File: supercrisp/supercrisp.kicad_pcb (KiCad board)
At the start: 2 copper layers, 140 x 91 mm, 114 parts, among them P1 USB_C_Plug_USB2.0, P2 USB_C_Plug_USB2.0, SW1 SW_Push, SW10 SW_Push, SW11 SW_Push, SW12 SW_Push, SW13 SW_Push, SW14 SW_Push, SW15 SW_Push, SW16 SW_Push, SW17 SW_Push, SW18 SW_Push, SW19 SW_Push, SW2 SW_Push, SW20 SW_Push, SW21 SW_Push, SW22 SW_Push, SW23 SW_Push, SW24 SW_Push, SW25 SW_Push, SW26 SW_Push, SW3 SW_Push, SW4 SW_Push, SW5 SW_Push, SW6 SW_Push, SW7 SW_Push, SW8 SW_Push, SW9 SW_Push, U1 STM32F072CBTx, U2 USBLC6-2SC6, U3 USBLC6-2SC6, U4 STM32F072CBTx

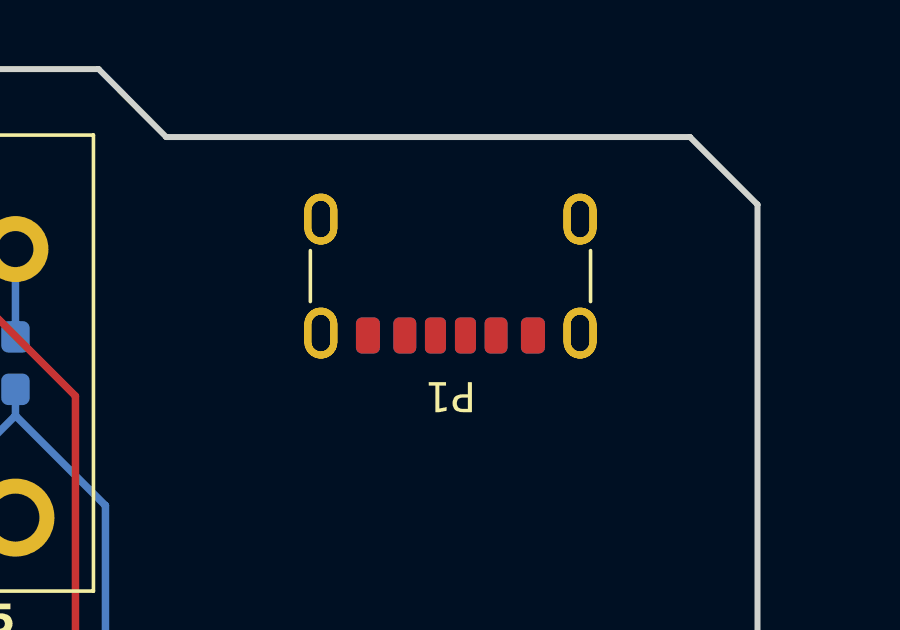
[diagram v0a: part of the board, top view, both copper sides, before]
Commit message: Start adding USB C connector circuit
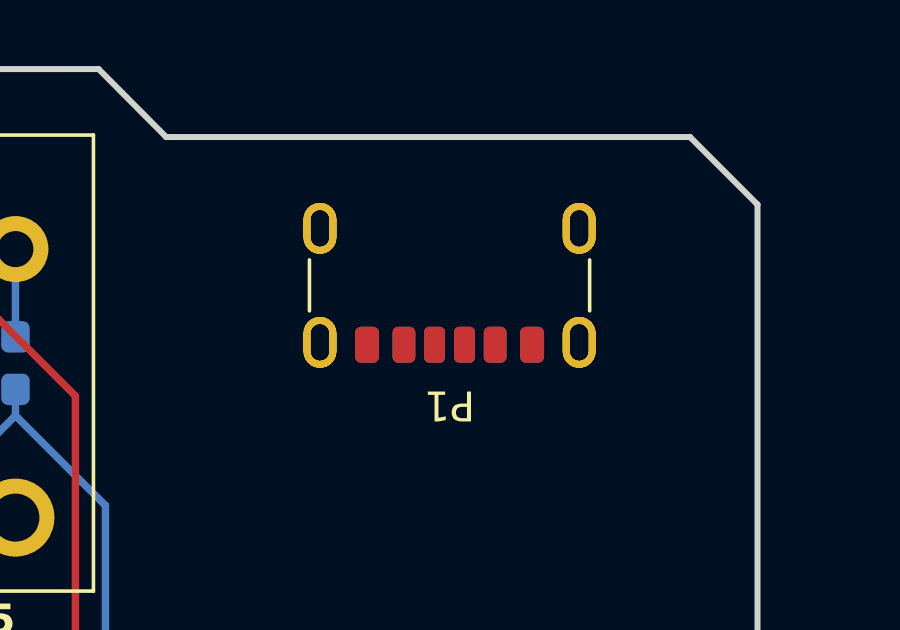
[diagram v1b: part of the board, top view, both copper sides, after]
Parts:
- moved P1 0.31 mm to (199.5, 44.3)
- moved P2 0.31 mm to (199.5, 44.3)
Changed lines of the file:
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@@
 	(footprint "Connector_USB:USB_C_Receptacle_GCT_USB4125-xx-x-0190_6P_TopMnt_Horizontal"
 		(layer "F.Cu")
-		(at 199.5 44 180)
+		(at 199.470019 44.30959 180)
 		(descr "USB Type C Receptacle, GCT, power-only, 6P, top mounted, horizontal, 3A, 1.9mm stake: https://gct.co/files/drawings/usb4125.pdf")
 		(tags "USB C Type-C receptacle power-only charging-only 6P 6C right angled")
@@
 	(footprint "Connector_USB:USB_C_Receptacle_GCT_USB4125-xx-x-0190_6P_TopMnt_Horizontal"
 		(layer "B.Cu")
-		(at 199.5 44)
+		(at 199.470019 44.30959)
 		(descr "USB Type C Receptacle, GCT, power-only, 6P, top mounted, horizontal, 3A, 1.9mm stake: https://gct.co/files/drawings/usb4125.pdf")
 		(tags "USB C Type-C receptacle power-only charging-only 6P 6C right angled")

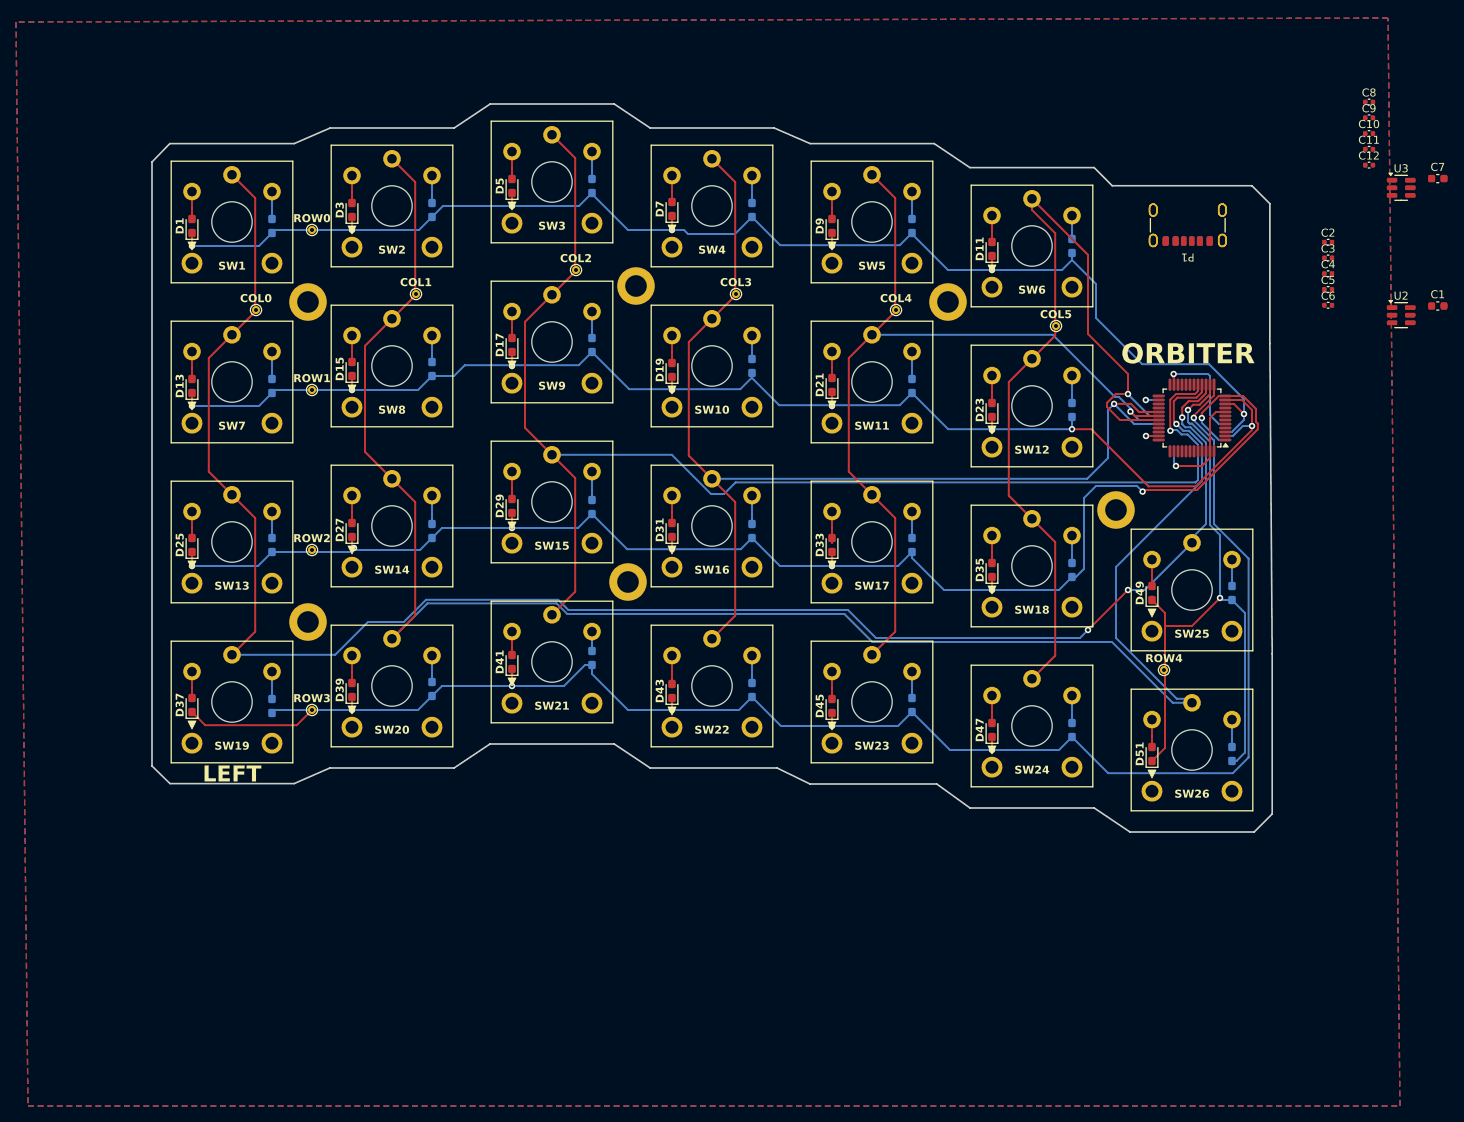
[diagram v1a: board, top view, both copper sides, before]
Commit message: Temp placement of switches and usb circuitry
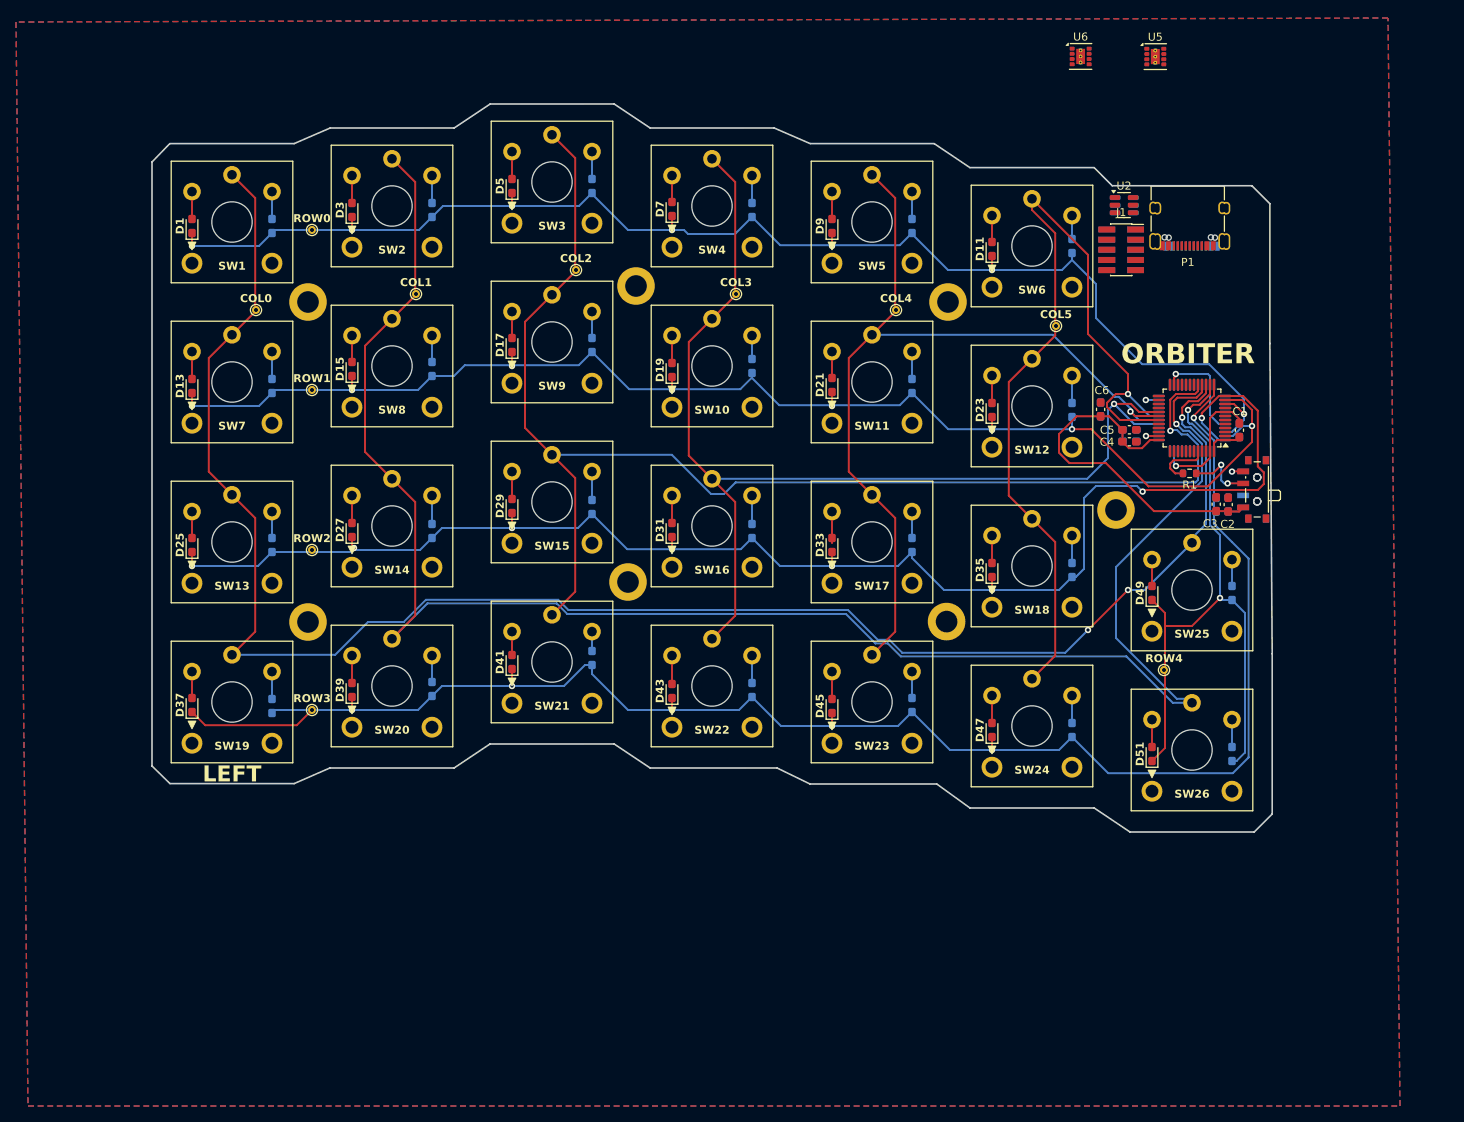
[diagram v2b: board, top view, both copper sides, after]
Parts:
- added H7: MountingHole_Pad, MountingHole_NoSilkscreen:MountingHole_2.7mm_M2.5_DIN965_Pad_reversible, F.Cu at (169.3, 95.0)
- added J1: SWD, Connector_PinSocket_1.27mm:PinSocket_2x05_P1.27mm_Vertical_SMD, F.Cu at (191.2, 48.5)
- added J2: SWD, Connector_PinSocket_1.27mm:PinSocket_2x05_P1.27mm_Vertical_SMD, B.Cu at (191.2, 48.5)
- added R1: 10k, Resistor_SMD:R_0603_1608Metric, F.Cu at (199.7, 76.4)
- added R2: 10k, Resistor_SMD:R_0603_1608Metric, B.Cu at (199.7, 76.4)
- added SW27: SW_SPDT, Button_Switch_SMD:SW_SPDT_PCM12, F.Cu at (207.8, 78.4)
- added SW28: SW_SPDT, Button_Switch_SMD:SW_SPDT_PCM12, B.Cu at (207.8, 78.4)
- added U5: TPS82140, Package_LGA:Texas_SIL0008D_MicroSiP-8-1EP_2.8x3mm_P0.65mm_EP1.1x1.9mm_ThermalVias, F.Cu at (195.4, 24.3)
- added U6: TPS82140, Package_LGA:Texas_SIL0008D_MicroSiP-8-1EP_2.8x3mm_P0.65mm_EP1.1x1.9mm_ThermalVias, F.Cu at (186.1, 24.3)
- C1: footprint Capacitor_SMD:C_0603_1608Metric -> Capacitor_SMD:C_0603_1608Metric_Pad1.08x0.95mm_HandSolder
- C10, C11, C12, C8, C9: footprint Capacitor_SMD:C_0402_1005Metric -> Capacitor_SMD:C_0603_1608Metric_Pad1.08x0.95mm_HandSolder; moved to B.Cu
- C2, C3, C4, C5, C6: footprint Capacitor_SMD:C_0402_1005Metric -> Capacitor_SMD:C_0603_1608Metric_Pad1.08x0.95mm_HandSolder
- C7: footprint Capacitor_SMD:C_0603_1608Metric -> Capacitor_SMD:C_0603_1608Metric_Pad1.08x0.95mm_HandSolder; moved to B.Cu
- P1, P2: footprint Connector_USB:USB_C_Receptacle_GCT_USB4125-xx-x-0190_6P_TopMnt_Horizontal -> Connector_USB:USB_C_Receptacle_XKB_U262-16XN-4BVC11
- U3: moved to B.Cu
- moved C8 53.3 mm to (204.5, 80.3), turned to 90 degrees
- moved C9 52.0 mm to (203.0, 80.3), turned to 90 degrees
- moved C10 48.7 mm to (192.2, 72.4), turned to 180 degrees
- moved C11 46.1 mm to (192.2, 71.0), turned to 180 degrees
- moved C12 45.4 mm to (188.6, 68.4), turned to 90 degrees
- moved C7 40.0 mm to (205.9, 71.0), turned to 90 degrees
- moved U2 37.3 mm to (191.5, 42.9)
- moved C2 35.1 mm to (204.5, 80.3), turned to 90 degrees
- moved U3 34.7 mm to (191.5, 42.9), turned to 180 degrees
- moved C3 33.8 mm to (203.0, 80.3), turned to 90 degrees
- moved C4 32.5 mm to (192.2, 72.5)
- moved C6 31.3 mm to (188.6, 68.4), turned to 90 degrees
- moved C5 30.4 mm to (192.2, 71.0)
- moved C1 29.3 mm to (205.9, 71.0), turned to 90 degrees
- moved P2 0.51 mm to (200.0, 44.4)
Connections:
- U1 pad 34: unconnected-(U1-PA13-Pad34) -> /MCU_TOP/SWDIO
- U1 pad 37: unconnected-(U1-PA14-Pad37) -> /MCU_TOP/SWCLK
- U1 pad 44: unconnected-(U1-BOOT0-Pad44) -> /MCU_TOP/BOOT0
- U1 pad 7: unconnected-(U1-NRST-Pad7) -> /MCU_TOP/NRST
- U4 pad 34: unconnected-(U4-PA13-Pad34) -> /MCU_BOTTOM/SWDIO
- U4 pad 37: unconnected-(U4-PA14-Pad37) -> /MCU_BOTTOM/SWCLK
- U4 pad 44: unconnected-(U4-BOOT0-Pad44) -> /MCU_BOTTOM/BOOT0
- U4 pad 7: unconnected-(U4-NRST-Pad7) -> /MCU_BOTTOM/NRST
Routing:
- net +3V3: track 0.00 -> 49.4 mm
- net Net-(SW27-B): track 0.00 -> 8.68 mm, vias 0 -> 2
- net /MCU_TOP/BOOT0: track 0.00 -> 7.09 mm
- net /T_MCU_ROW2: track 183.2 -> 188.3 mm
- net GND: track 30.6 -> 34.6 mm, vias 4 -> 5
- net /T_MCU_COL0: track 221.0 -> 222.5 mm
- net /T_MCU_ROW1: track 170.7 -> 171.6 mm

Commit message: Add step down circuit in schematic editor
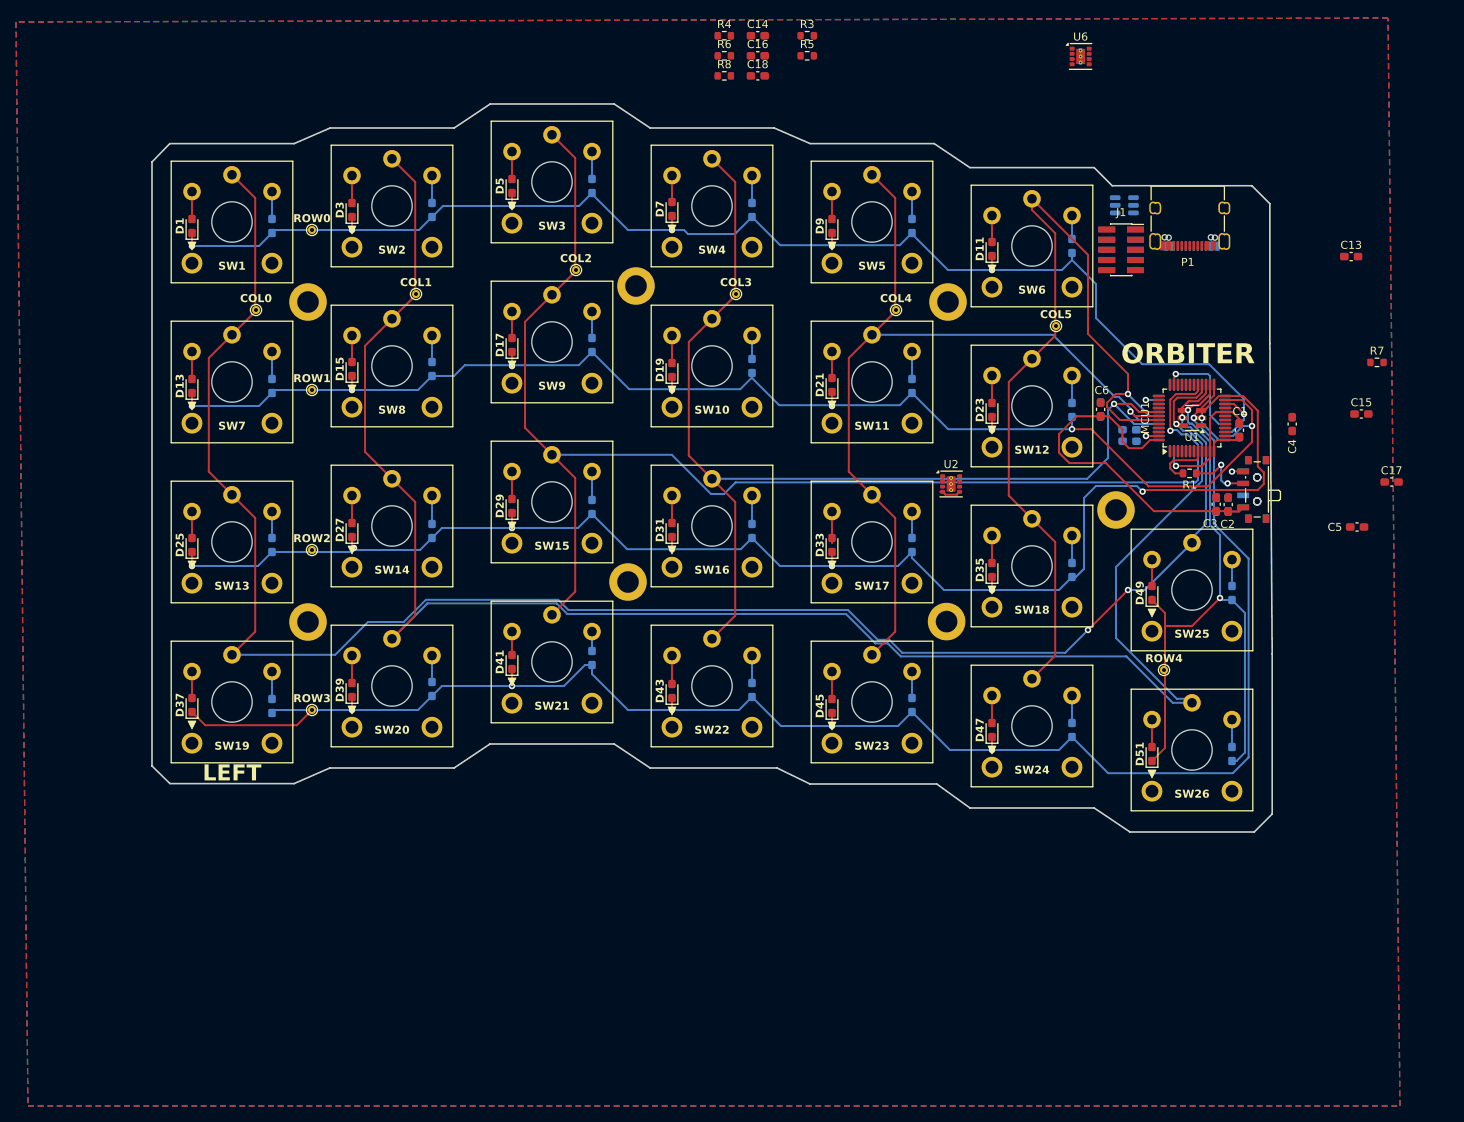
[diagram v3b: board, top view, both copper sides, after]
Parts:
- removed U4: STM32F072CBTx, Package_QFP:LQFP-48_7x7mm_P0.5mm
- removed U5: TPS82140, Package_LGA:Texas_SIL0008D_MicroSiP-8-1EP_2.8x3mm_P0.65mm_EP1.1x1.9mm_ThermalVias
- added C13: 100n, Capacitor_SMD:C_0603_1608Metric_Pad1.08x0.95mm_HandSolder, F.Cu at (219.9, 49.3)
- added C14: 430pF, Capacitor_SMD:C_0603_1608Metric_Pad1.08x0.95mm_HandSolder, F.Cu at (145.7, 21.7)
- added C15: 100n, Capacitor_SMD:C_0603_1608Metric_Pad1.08x0.95mm_HandSolder, F.Cu at (221.2, 69.0)
- added C16: 22uF, Capacitor_SMD:C_0603_1608Metric_Pad1.08x0.95mm_HandSolder, F.Cu at (145.7, 24.2)
- added C17: 100n, Capacitor_SMD:C_0603_1608Metric_Pad1.08x0.95mm_HandSolder, F.Cu at (224.9, 77.5)
- added C18: 22uF, Capacitor_SMD:C_0603_1608Metric_Pad1.08x0.95mm_HandSolder, F.Cu at (145.7, 26.7)
- added MCU1: STM32F072CBTx, Package_QFP:LQFP-48_7x7mm_P0.5mm, F.Cu at (200.0, 69.5)
- added MCU2: STM32F072CBTx, Package_QFP:LQFP-48_7x7mm_P0.5mm, B.Cu at (200.0, 69.5)
- added R3: 309k, Resistor_SMD:R_0603_1608Metric, F.Cu at (151.9, 21.7)
- added R4: 100k, Resistor_SMD:R_0603_1608Metric, F.Cu at (141.5, 21.7)
- added R5: 100k, Resistor_SMD:R_0603_1608Metric, F.Cu at (151.9, 24.2)
- added R6: 309k, Resistor_SMD:R_0603_1608Metric, F.Cu at (141.5, 24.2)
- added R7: 10k, Resistor_SMD:R_0603_1608Metric, F.Cu at (223.1, 62.5)
- added R8: 100k, Resistor_SMD:R_0603_1608Metric, F.Cu at (141.5, 26.7)
- C1: value 4u7 -> 22uF
- C2: value 100n -> 430pF
- C3: value 100n -> 22uF
- C4: value 100n -> 4u7
- R1: value 10k -> 100k
- U1: value STM32F072CBTx -> USBLC6-2SC6; footprint Package_QFP:LQFP-48_7x7mm_P0.5mm -> Package_TO_SOT_SMD:SOT-23-6
- U2: value USBLC6-2SC6 -> TPS82140; footprint Package_TO_SOT_SMD:SOT-23-6 -> Package_LGA:Texas_SIL0008D_MicroSiP-8-1EP_2.8x3mm_P0.65mm_EP1.1x1.9mm_ThermalVias
- moved U2 41.0 mm to (169.9, 77.8)
- moved C5 30.9 mm to (220.6, 83.1)
- moved C4 20.5 mm to (212.5, 70.3), turned to 90 degrees
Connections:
- C1 pad 1: +3V3 -> /MCU_TOP/VBUS
- C10 pad 1: +3V3 -> /MCU_BOTTOM/VOUT_3V3
- C11 pad 1: +3V3 -> /MCU_BOTTOM/VOUT_3V3
- C12 pad 1: +3V3 -> /MCU_BOTTOM/VOUT_3V3
- C2 pad 1: +3V3 -> Net-(U2-SS/TR)
- C3 pad 1: +3V3 -> /MCU_TOP/VOUT_3V3
- C4 pad 1: +3V3 -> /MCU_TOP/VOUT_3V3
- C5 pad 1: +3V3 -> /MCU_TOP/VOUT_3V3
- C6 pad 1: +3V3 -> /MCU_TOP/VOUT_3V3
- C7 pad 1: +3V3 -> /MCU_BOTTOM/VOUT_3V3
- C8 pad 1: +3V3 -> /MCU_BOTTOM/VOUT_3V3
- C9 pad 1: +3V3 -> /MCU_BOTTOM/VOUT_3V3
- J1 pad 1: +3V3 -> /MCU_TOP/VOUT_3V3
- J2 pad 1: +3V3 -> /MCU_BOTTOM/VOUT_3V3
- P1 pad A4: +5V -> /MCU_TOP/VBUS
- P1 pad A9: +5V -> /MCU_TOP/VBUS
- P1 pad B4: +5V -> /MCU_TOP/VBUS
- P1 pad B9: +5V -> /MCU_TOP/VBUS
- P2 pad A4: +5V -> /MCU_BOTTOM/VBUS
- P2 pad A9: +5V -> /MCU_BOTTOM/VBUS
- P2 pad B4: +5V -> /MCU_BOTTOM/VBUS
- P2 pad B9: +5V -> /MCU_BOTTOM/VBUS
- R1 pad 1: Net-(SW27-B) -> /MCU_TOP/VOUT_3V3
- R1 pad 2: /MCU_TOP/BOOT0 -> Net-(U2-PG)
- SW27 pad 1: +3V3 -> /MCU_TOP/VOUT_3V3
- SW28 pad 1: +3V3 -> /MCU_BOTTOM/VOUT_3V3
- U1 pad 1: +3V3 -> /MCU_TOP/USB_CONN_D-
- U1 pad 2: unconnected-(U1-PC13-Pad2) -> GND
- U1 pad 3: unconnected-(U1-PC14-Pad3) -> /MCU_TOP/USB_CONN_D+
- U1 pad 4: unconnected-(U1-PC15-Pad4) -> /MCU_TOP/USB_D+
- U1 pad 5: unconnected-(U1-PF0-Pad5) -> /MCU_TOP/VBUS
- U1 pad 6: unconnected-(U1-PF1-Pad6) -> /MCU_TOP/USB_D-
- U2 pad 1: /MCU_TOP/USB_CONN_D- -> /MCU_TOP/VBUS
- U2 pad 2: GND -> /MCU_TOP/VBUS
- U2 pad 3: /MCU_TOP/USB_CONN_D+ -> GND
- U2 pad 4: /MCU_TOP/USB_D+ -> /MCU_TOP/VOUT_3V3
- U2 pad 5: +5V -> /MCU_TOP/VOUT_3V3
- U2 pad 6: /MCU_TOP/USB_D- -> Net-(U2-FB)
- U3 pad 5: +5V -> /MCU_BOTTOM/VBUS
- U6 pad 1: unconnected-(U6-EN-Pad1) -> /MCU_BOTTOM/VBUS
- U6 pad 2: unconnected-(U6-VIN-Pad2) -> /MCU_BOTTOM/VBUS
- U6 pad 3: Net-(U6-GND-Pad3) -> GND
- U6 pad 4: Net-(U6-VOUT-Pad4) -> /MCU_BOTTOM/VOUT_3V3
- U6 pad 5: Net-(U6-VOUT-Pad4) -> /MCU_BOTTOM/VOUT_3V3
- U6 pad 6: unconnected-(U6-FB-Pad6) -> Net-(U6-FB)
- U6 pad 7: unconnected-(U6-PG-Pad7) -> Net-(U6-PG)
- U6 pad 8: unconnected-(U6-SS/TR-Pad8) -> Net-(U6-SS/TR)
- U6 pad 9: Net-(U6-GND-Pad3) -> GND
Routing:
- net +3V3: track 49.4 -> 0.00 mm
- net (no net): track 0.00 -> 49.4 mm
- net /MCU_TOP/VOUT_3V3: track 0.00 -> 2.73 mm
- net /MCU_TOP/VBUS: track 0.00 -> 0.65 mm
